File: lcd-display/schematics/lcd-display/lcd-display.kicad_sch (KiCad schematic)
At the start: 12 parts, among them U1 74LS04, U2 74LS08, U3 74LS245, U4 74LS32

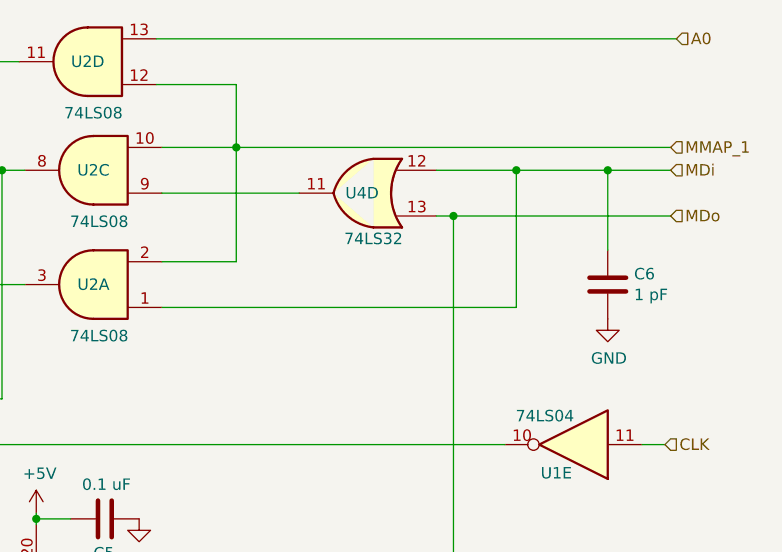
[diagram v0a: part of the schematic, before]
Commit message: KiCad v6 update
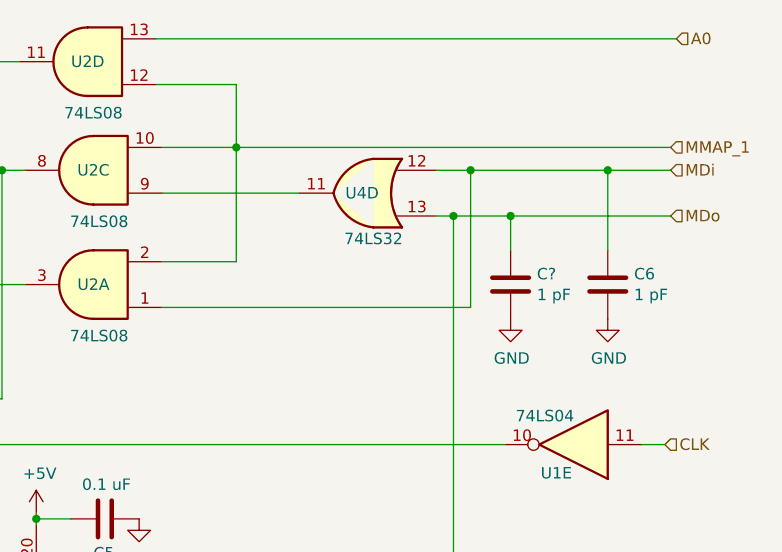
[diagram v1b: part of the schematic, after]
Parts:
- added C?: 1 pF, symbol Device:C
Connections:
- net GND: now also C?.2
- net MDo: now also C?.1
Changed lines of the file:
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@@
   (junction (at 203.835 31.115) (diameter 0) (color 0 0 0 0)
   )
-  (junction (at 234.95 33.655) (diameter 0) (color 0 0 0 0)
-  )
   (junction (at 73.66 48.26) (diameter 0) (color 0 0 0 0)
   )
@@
   (junction (at 60.325 60.96) (diameter 0) (color 0 0 0 0)
   )
+  (junction (at 234.315 38.735) (diameter 0) (color 0 0 0 0)
+  )
   (junction (at 73.66 67.945) (diameter 0) (color 0 0 0 0)
   )
@@
   (junction (at 57.15 167.64) (diameter 0) (color 0 0 0 0)
   )
+  (junction (at 229.87 33.655) (diameter 0) (color 0 0 0 0)
+  )
   (wire (pts (xy 116.84 33.655) (xy 116.84 113.665))
     (stroke (width 0) (type default) (color 0 0 0 0))
@@
     (stroke (width 0) (type default) (color 0 0 0 0))
   )
+  (wire (pts (xy 229.87 33.655) (xy 226.06 33.655))
+    (stroke (width 0) (type default) (color 0 0 0 0))
+  )
+  (wire (pts (xy 229.87 33.655) (xy 245.11 33.655))
+    (stroke (width 0) (type default) (color 0 0 0 0))
+  )
   (wire (pts (xy 181.61 113.665) (xy 181.61 115.57))
     (stroke (width 0) (type default) (color 0 0 0 0))
@@
     (stroke (width 0) (type default) (color 0 0 0 0))
   )
-  (wire (pts (xy 234.95 33.655) (xy 234.95 48.895))
+  (wire (pts (xy 229.87 33.655) (xy 229.87 48.895))
     (stroke (width 0) (type default) (color 0 0 0 0))
   )
@@
     (stroke (width 0) (type default) (color 0 0 0 0))
   )
-  (wire (pts (xy 227.965 38.735) (xy 252.095 38.735))
-    (stroke (width 0) (type default) (color 0 0 0 0))
-  )
-  (wire (pts (xy 195.58 48.895) (xy 234.95 48.895))
+  (wire (pts (xy 227.965 38.735) (xy 234.315 38.735))
+    (stroke (width 0) (type default) (color 0 0 0 0))
+  )
+  (wire (pts (xy 195.58 48.895) (xy 229.87 48.895))
     (stroke (width 0) (type default) (color 0 0 0 0))
   )
@@
     (stroke (width 0) (type default) (color 0 0 0 0))
   )
+  (wire (pts (xy 234.315 38.735) (xy 234.315 42.545))
+    (stroke (width 0) (type default) (color 0 0 0 0))
+  )
   (wire (pts (xy 66.675 70.485) (xy 66.675 64.77))
     (stroke (width 0) (type default) (color 0 0 0 0))
   )
+  (wire (pts (xy 234.315 38.735) (xy 252.095 38.735))
+    (stroke (width 0) (type default) (color 0 0 0 0))
+  )
   (wire (pts (xy 121.92 46.355) (xy 127.635 46.355))
     (stroke (width 0) (type default) (color 0 0 0 0))
@@
     (stroke (width 0) (type default) (color 0 0 0 0))
   )
-  (wire (pts (xy 245.11 33.655) (xy 234.95 33.655))
-    (stroke (width 0) (type default) (color 0 0 0 0))
-  )
   (wire (pts (xy 73.66 100.965) (xy 73.66 67.945))
     (stroke (width 0) (type default) (color 0 0 0 0))
   )
   (wire (pts (xy 49.53 158.115) (xy 49.53 147.955))
-    (stroke (width 0) (type default) (color 0 0 0 0))
-  )
-  (wire (pts (xy 234.95 33.655) (xy 226.06 33.655))
     (stroke (width 0) (type default) (color 0 0 0 0))
   )
@@
     (pin "2")
   )
+  (symbol (lib_id "power:GND") (at 234.315 50.165 0) (unit 1)
+    (in_bom yes) (on_board yes)
+    (property "Reference" "#PWR?" (id 0) (at 234.315 56.515 0)
+      (effects (font (size 1.27 1.27)) hide)
+    )
+    (property "Value" "GND" (id 1) (at 234.442 54.5592 0))
+    (property "Footprint" "" (id 2) (at 234.315 50.165 0)
+      (effects (font (size 1.27 1.27)) hide)
+    )
+    (property "Datasheet" "" (id 3) (at 234.315 50.165 0)
+      (effects (font (size 1.27 1.27)) hide)
+    )
+    (pin "1")
+  )
+  (symbol (lib_id "Device:C") (at 234.315 46.355 0) (unit 1)
+    (in_bom yes) (on_board yes)
+    (property "Reference" "C?" (id 0) (at 237.236 45.1866 0)
+      (effects (font (size 1.27 1.27)) (justify left))
+    )
+    (property "Value" "1 pF" (id 1) (at 237.236 47.498 0)
+      (effects (font (size 1.27 1.27)) (justify left))
+    )
+    (property "Footprint" "" (id 2) (at 235.2802 50.165 0)
+      (effects (font (size 1.27 1.27)) hide)
+    )
+    (property "Datasheet" "~" (id 3) (at 234.315 46.355 0)
+      (effects (font (size 1.27 1.27)) hide)
+    )
+    (pin "1")
+    (pin "2")
+  )
   (sheet_instances
     (path "/" (page "1"))
@@
       (reference "#PWR08") (unit 1) (value "GND") (footprint "")
     )
+    (path "/0ae0dde3-a8f0-402c-b308-f4d09e8aaec5"
+      (reference "#PWR?") (unit 1) (value "GND") (footprint "")
+    )
     (path "/00000000-0000-0000-0000-000061d87343"
       (reference "C1") (unit 1) (value "0.1 uF") (footprint "")
@@
       (reference "C6") (unit 1) (value "1 pF") (footprint "")
     )
+    (path "/9a7ade3c-a81d-4038-a57c-b220b9c3cd90"
+      (reference "C?") (unit 1) (value "1 pF") (footprint "")
+    )
     (path "/00000000-0000-0000-0000-000061c95bc7"

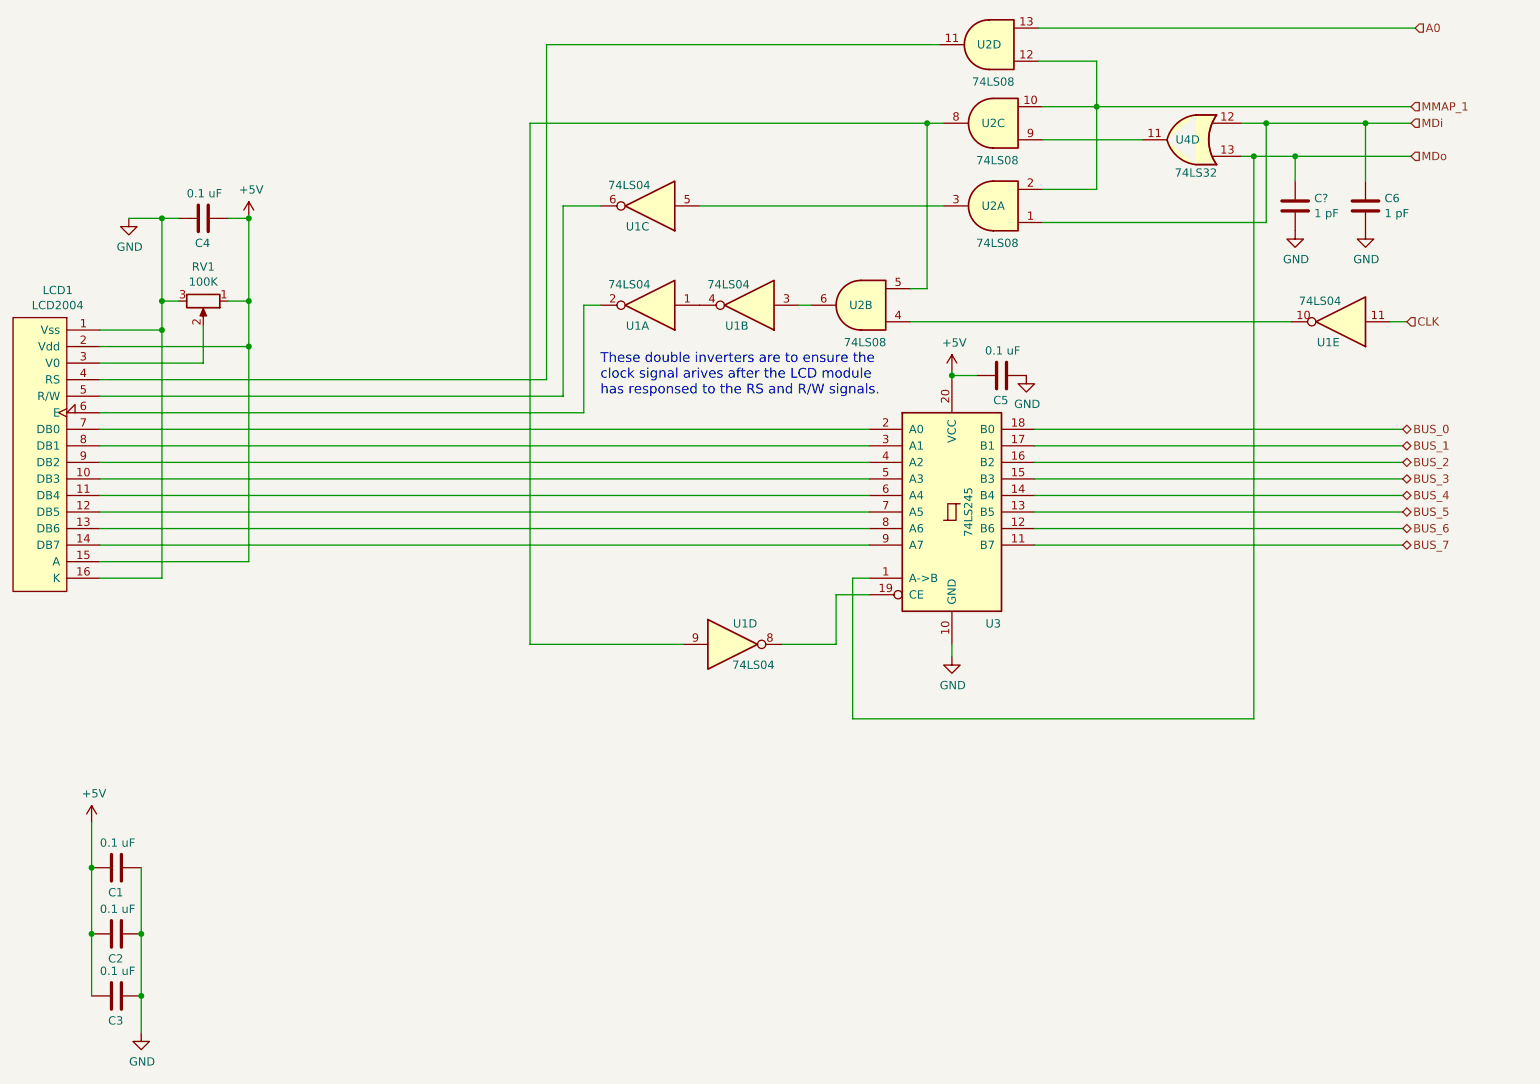
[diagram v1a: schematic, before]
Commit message: adjust CLK signal timing
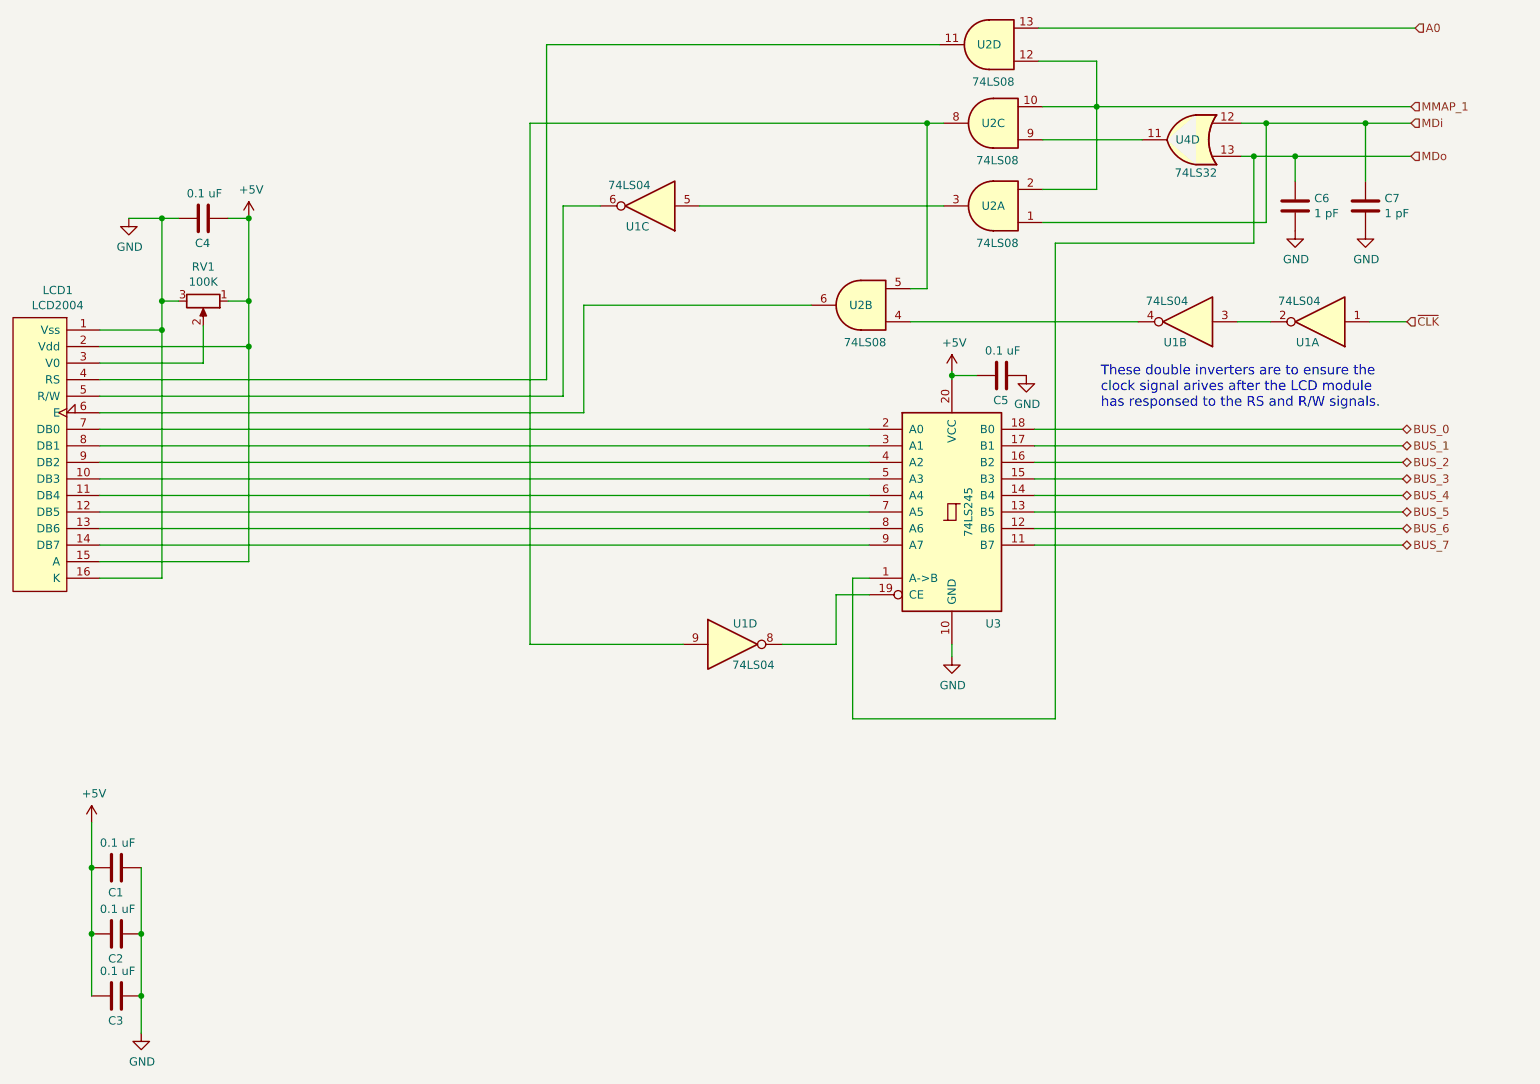
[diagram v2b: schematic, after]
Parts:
- removed unit 5 of U1
- gave numbers to parts that had none: 1
- renumbered C6 to C7
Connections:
- net at LCD1.6 (E): now also U2.6; no longer U1.2
- net at U2.4: now also U1.4
- net at U1.3: now also U1.2; no longer U2.6
- net ~{CLK}: now reaches U1.1
- net ~{CLK}: no longer U1.4
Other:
- moved on the sheet: U1A, U1B
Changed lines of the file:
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@@
+    (stroke (width 0) (type default) (color 0 0 0 0))
+  )
+  (wire (pts (xy 245.745 64.135) (xy 251.46 64.135))
     (stroke (width 0) (type default) (color 0 0 0 0))
   )
@@
     (stroke (width 0) (type default) (color 0 0 0 0))
   )
-  (wire (pts (xy 227.965 125.095) (xy 227.965 38.735))
+  (wire (pts (xy 227.965 52.07) (xy 197.485 52.07))
     (stroke (width 0) (type default) (color 0 0 0 0))
   )
@@
     (stroke (width 0) (type default) (color 0 0 0 0))
   )
-  (wire (pts (xy 175.26 64.135) (xy 233.68 64.135))
-    (stroke (width 0) (type default) (color 0 0 0 0))
-  )
   (wire (pts (xy 177.8 33.655) (xy 177.8 59.055))
     (stroke (width 0) (type default) (color 0 0 0 0))
@@
     (stroke (width 0) (type default) (color 0 0 0 0))
   )
+  (wire (pts (xy 175.26 64.135) (xy 210.185 64.135))
+    (stroke (width 0) (type default) (color 0 0 0 0))
+  )
   (wire (pts (xy 252.095 33.655) (xy 245.11 33.655))
     (stroke (width 0) (type default) (color 0 0 0 0))
@@
     (stroke (width 0) (type default) (color 0 0 0 0))
   )
-  (wire (pts (xy 248.92 64.135) (xy 251.46 64.135))
-    (stroke (width 0) (type default) (color 0 0 0 0))
-  )
   (wire (pts (xy 60.325 48.26) (xy 55.245 48.26))
     (stroke (width 0) (type default) (color 0 0 0 0))
@@
     (stroke (width 0) (type default) (color 0 0 0 0))
   )
-  (wire (pts (xy 125.095 61.595) (xy 127.635 61.595))
+  (wire (pts (xy 225.425 64.135) (xy 230.505 64.135))
     (stroke (width 0) (type default) (color 0 0 0 0))
   )
@@
     (stroke (width 0) (type default) (color 0 0 0 0))
   )
-  (wire (pts (xy 166.37 125.095) (xy 227.965 125.095))
+  (wire (pts (xy 166.37 125.095) (xy 197.485 125.095))
     (stroke (width 0) (type default) (color 0 0 0 0))
   )
@@
     (stroke (width 0) (type default) (color 0 0 0 0))
   )
+  (wire (pts (xy 227.965 52.07) (xy 227.965 38.735))
+    (stroke (width 0) (type default) (color 0 0 0 0))
+  )
   (wire (pts (xy 57.15 147.955) (xy 57.15 158.115))
     (stroke (width 0) (type default) (color 0 0 0 0))
@@
     (stroke (width 0) (type default) (color 0 0 0 0))
   )
-  (wire (pts (xy 158.115 61.595) (xy 160.02 61.595))
+  (wire (pts (xy 125.095 61.595) (xy 160.02 61.595))
     (stroke (width 0) (type default) (color 0 0 0 0))
   )
@@
     (stroke (width 0) (type default) (color 0 0 0 0))
   )
+  (wire (pts (xy 197.485 52.07) (xy 197.485 125.095))
+    (stroke (width 0) (type default) (color 0 0 0 0))
+  )
   (text "These double inverters are to ensure the\nclock signal arives after the LCD module \nhas responsed to the RS and R/W signals."
-    (at 127.635 75.565 0)
+    (at 204.47 77.47 0)
     (effects (font (size 1.4986 1.4986)) (justify left bottom))
   )
@@
     (effects (font (size 1.27 1.27)) (justify left))
   )
-  (hierarchical_label "CLK" (shape input) (at 251.46 64.135 0)
+  (hierarchical_label "~{CLK}" (shape input) (at 251.46 64.135 0)
     (effects (font (size 1.27 1.27)) (justify left))
   )
@@
   (symbol (lib_id "Device:C") (at 245.11 46.355 0) (unit 1)
     (in_bom yes) (on_board yes)
-    (property "Reference" "C6" (id 0) (at 248.031 45.1866 0)
+    (property "Reference" "C7" (id 0) (at 248.031 45.1866 0)
       (effects (font (size 1.27 1.27)) (justify left))
     )
@@
   (symbol (lib_id "power:GND") (at 245.11 50.165 0) (unit 1)
     (in_bom yes) (on_board yes)
-    (property "Reference" "#PWR08" (id 0) (at 245.11 56.515 0)
+    (property "Reference" "#PWR09" (id 0) (at 245.11 56.515 0)
       (effects (font (size 1.27 1.27)) hide)
     )
@@
     (pin "9")
   )
-  (symbol (lib_id "74xx:74LS04") (at 241.3 64.135 180) (unit 5)
-    (in_bom yes) (on_board yes)
-    (property "Reference" "U1" (id 0) (at 239.395 67.31 0))
-    (property "Value" "74LS04" (id 1) (at 238.125 60.96 0))
-    (property "Footprint" "" (id 2) (at 241.3 64.135 0)
-      (effects (font (size 1.27 1.27)) hide)
-    )
-    (property "Datasheet" "http://www.ti.com/lit/gpn/sn74LS04" (id 3) (at 241.3 64.135 0)
-      (effects (font (size 1.27 1.27)) hide)
-    )
-    (pin "10")
-    (pin "11")
-  )
   (symbol (lib_id "Device:C") (at 53.34 147.955 270) (unit 1)
     (in_bom yes) (on_board yes)
@@
     (pin "6")
   )
-  (symbol (lib_id "74xx:74LS04") (at 150.495 61.595 180) (unit 2)
-    (in_bom yes) (on_board yes)
-    (property "Reference" "U1" (id 0) (at 148.59 64.77 0))
-    (property "Value" "74LS04" (id 1) (at 147.32 58.42 0))
-    (property "Footprint" "" (id 2) (at 150.495 61.595 0)
-      (effects (font (size 1.27 1.27)) hide)
-    )
-    (property "Datasheet" "http://www.ti.com/lit/gpn/sn74LS04" (id 3) (at 150.495 61.595 0)
+  (symbol (lib_id "74xx:74LS04") (at 217.805 64.135 180) (unit 2)
+    (in_bom yes) (on_board yes)
+    (property "Reference" "U1" (id 0) (at 215.9 67.31 0))
+    (property "Value" "74LS04" (id 1) (at 214.63 60.96 0))
+    (property "Footprint" "" (id 2) (at 217.805 64.135 0)
+      (effects (font (size 1.27 1.27)) hide)
+    )
+    (property "Datasheet" "http://www.ti.com/lit/gpn/sn74LS04" (id 3) (at 217.805 64.135 0)
       (effects (font (size 1.27 1.27)) hide)
     )
@@
     (pin "4")
   )
-  (symbol (lib_id "74xx:74LS04") (at 135.255 61.595 180) (unit 1)
-    (in_bom yes) (on_board yes)
-    (property "Reference" "U1" (id 0) (at 133.35 64.77 0))
-    (property "Value" "74LS04" (id 1) (at 132.08 58.42 0))
-    (property "Footprint" "" (id 2) (at 135.255 61.595 0)
-      (effects (font (size 1.27 1.27)) hide)
-    )
-    (property "Datasheet" "http://www.ti.com/lit/gpn/sn74LS04" (id 3) (at 135.255 61.595 0)
+  (symbol (lib_id "74xx:74LS04") (at 238.125 64.135 180) (unit 1)
+    (in_bom yes) (on_board yes)
+    (property "Reference" "U1" (id 0) (at 236.22 67.31 0))
+    (property "Value" "74LS04" (id 1) (at 234.95 60.96 0))
+    (property "Footprint" "" (id 2) (at 238.125 64.135 0)
+      (effects (font (size 1.27 1.27)) hide)
+    )
+    (property "Datasheet" "http://www.ti.com/lit/gpn/sn74LS04" (id 3) (at 238.125 64.135 0)
       (effects (font (size 1.27 1.27)) hide)
     )
@@
   (symbol (lib_id "power:GND") (at 234.315 50.165 0) (unit 1)
     (in_bom yes) (on_board yes)
-    (property "Reference" "#PWR?" (id 0) (at 234.315 56.515 0)
+    (property "Reference" "#PWR08" (id 0) (at 234.315 56.515 0)
       (effects (font (size 1.27 1.27)) hide)
     )
@@
   (symbol (lib_id "Device:C") (at 234.315 46.355 0) (unit 1)
     (in_bom yes) (on_board yes)
-    (property "Reference" "C?" (id 0) (at 237.236 45.1866 0)
+    (property "Reference" "C6" (id 0) (at 237.236 45.1866 0)
       (effects (font (size 1.27 1.27)) (justify left))
     )
@@
       (reference "#PWR07") (unit 1) (value "GND") (footprint "")
     )
+    (path "/0ae0dde3-a8f0-402c-b308-f4d09e8aaec5"
+      (reference "#PWR08") (unit 1) (value "GND") (footprint "")
+    )
     (path "/00000000-0000-0000-0000-000061d0faec"
-      (reference "#PWR08") (unit 1) (value "GND") (footprint "")
-    )
-    (path "/0ae0dde3-a8f0-402c-b308-f4d09e8aaec5"
-      (reference "#PWR?") (unit 1) (value "GND") (footprint "")
+      (reference "#PWR09") (unit 1) (value "GND") (footprint "")
     )
     (path "/00000000-0000-0000-0000-000061d87343"
@@
       (reference "C5") (unit 1) (value "0.1 uF") (footprint "")
     )
+    (path "/9a7ade3c-a81d-4038-a57c-b220b9c3cd90"
+      (reference "C6") (unit 1) (value "1 pF") (footprint "")
+    )
     (path "/00000000-0000-0000-0000-000061d0eeb6"
-      (reference "C6") (unit 1) (value "1 pF") (footprint "")
-    )
-    (path "/9a7ade3c-a81d-4038-a57c-b220b9c3cd90"
-      (reference "C?") (unit 1) (value "1 pF") (footprint "")
+      (reference "C7") (unit 1) (value "1 pF") (footprint "")
     )
     (path "/00000000-0000-0000-0000-000061c95bc7"
@@
       (reference "U1") (unit 4) (value "74LS04") (footprint "")
     )
-    (path "/00000000-0000-0000-0000-000061d73754"
-      (reference "U1") (unit 5) (value "74LS04") (footprint "")
-    )
     (path "/00000000-0000-0000-0000-000061d9c6fa"
